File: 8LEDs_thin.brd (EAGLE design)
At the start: 25.1 x 52.1 mm, 10 parts

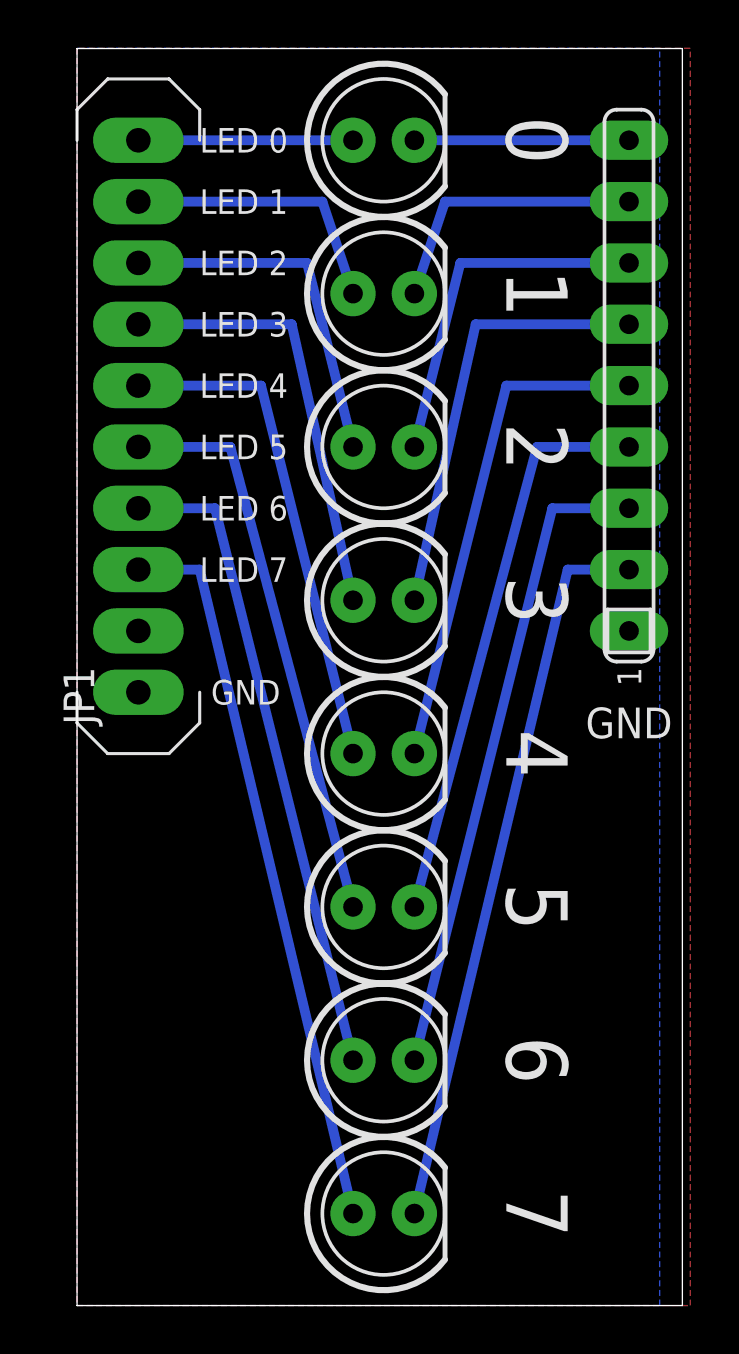
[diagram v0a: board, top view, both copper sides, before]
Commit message: added power jumper to serial: mx8 spider
other tweaks include stuff with the 8LED modules
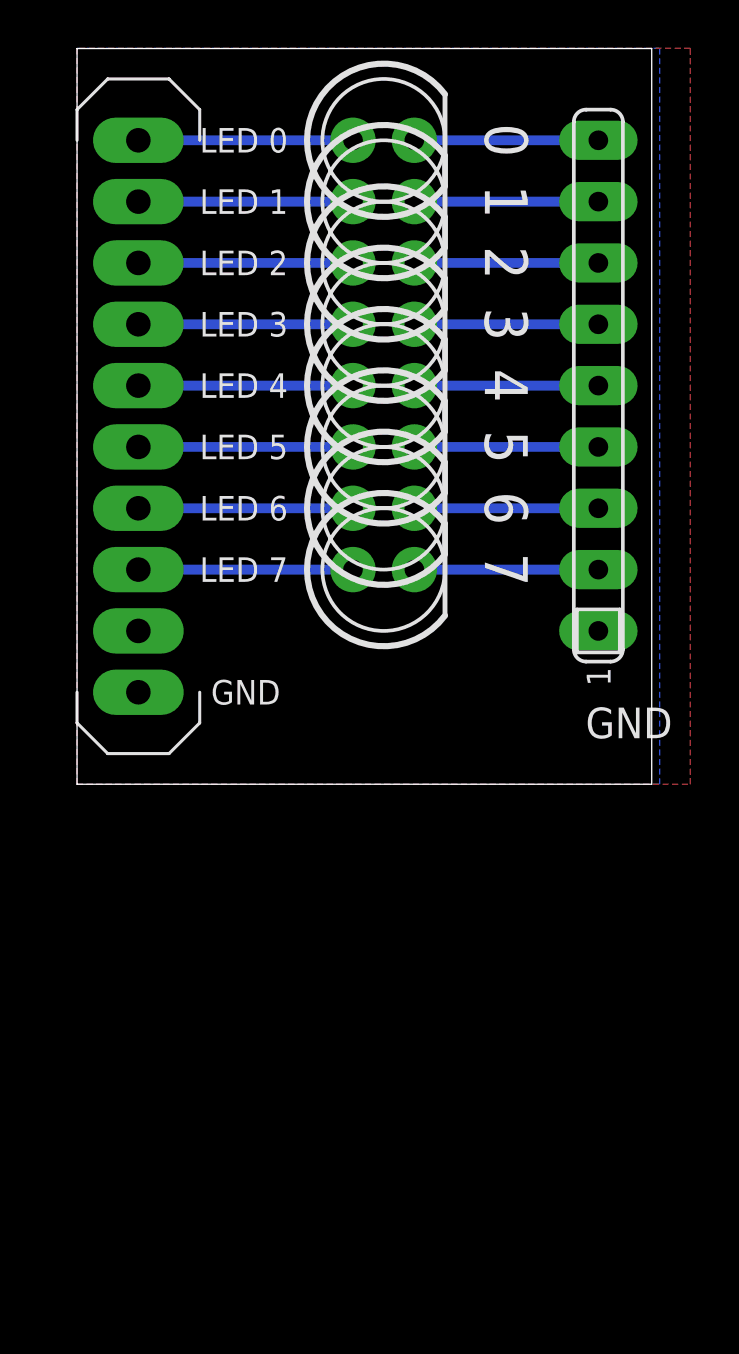
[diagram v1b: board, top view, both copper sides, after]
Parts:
- moved LED8 26.7 mm to (71.1, 40.6)
- moved LED7 22.9 mm to (71.1, 43.2)
- moved LED6 19.0 mm to (71.1, 45.7)
- moved LED5 15.2 mm to (71.1, 48.3)
- moved LED4 11.4 mm to (71.1, 50.8)
- moved LED3 7.62 mm to (71.1, 53.3)
- moved LED2 3.81 mm to (71.1, 55.9)
- moved RN1 1.27 mm to (80.0, 48.3)
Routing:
- net N$8: track 30.0 -> 7.62 mm
- net N$16: track 30.0 -> 8.89 mm
- net N$7: track 26.7 -> 7.62 mm
- net N$15: track 26.7 -> 8.89 mm
- net N$6: track 23.5 -> 7.62 mm
- net N$14: track 23.5 -> 8.89 mm
- net N$5: track 20.8 -> 7.62 mm
- net N$13: track 20.8 -> 8.89 mm
- net N$4: track 18.1 -> 7.62 mm
- net N$12: track 18.1 -> 8.89 mm
- net N$3: track 14.8 -> 7.62 mm
- net N$11: track 14.8 -> 8.89 mm
- net N$2: track 11.6 -> 7.62 mm
- net N$10: track 11.6 -> 8.89 mm
- net N$1: track 8.89 -> 7.62 mm
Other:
- board size 25.1 x 52.1 mm -> 23.8 x 30.5 mm
